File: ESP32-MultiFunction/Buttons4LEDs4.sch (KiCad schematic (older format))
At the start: 0 parts

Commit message: Working on ESP32-MultiFunction.
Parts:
- added C12: .1 uf, Capacitors_SMD:C_0603, symbol C
- added C13, C14, C15, C16: 10 nf, Capacitors_SMD:C_0603, symbol C_Small
- added R15, R17, R19, R21: R, Resistors_THT:R_Axial_DIN0207_L6.3mm_D2.5mm_P7.62mm_Horizontal, symbol R
- added R16, R18, R20, R22: 1.5K Ohms, Resistors_SMD:R_0603, symbol R
- added R23, R24, R25, R26: 10K Ohms, Resistors_SMD:R_0603, symbol R
- added Term6: +12 1 2 3 4 GND, Connectors_Terminal_Blocks:TerminalBlock_Pheonix_MPT-2.54mm_6pol, symbol Screw_Terminal_01x06
- added Term7: 1 2 3 4 GND, Connectors_Terminal_Blocks:TerminalBlock_Pheonix_MPT-2.54mm_5pol, symbol Screw_Terminal_01x05
- added U11, U12: TC4426, Housings_SOIC:SOIC-8_3.9x4.9mm_Pitch1.27mm, symbol TC4426
- added U13: 74HCT14, Housings_SOIC:SOIC-14_3.9x8.7mm_Pitch1.27mm, symbol 74HC14
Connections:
- new net: C13.1, R23.2, Term7.1 (Pin_1), U13.5
- new net: C14.1, R24.2, Term7.2 (Pin_2), U13.9
- new net: C16.1, R26.2, Term7.3 (Pin_3), U13.11
- new net: C15.1, R25.2, Term7.4 (Pin_4), U13.13
- new net: R15.2, R16.2, U11.7 (Out)
- new net: R17.2, R18.2, U11.5 (Out)
- new net: R19.2, R20.2, U12.7 (Out)
- new net: R21.2, R22.2, U12.5 (Out)
- new net: R15.1, R16.1, Term6.2 (Pin_2)
- new net: R17.1, R18.1, Term6.3 (Pin_3)
- new net: R19.1, R20.1, Term6.4 (Pin_4)
- new net: R21.1, R22.1, Term6.5 (Pin_5)
- new net +12V: Term6.1 (Pin_1), U11.6 (Vdd), U11.6 (Vdd), U12.6 (Vdd), U12.6 (Vdd)
- new net +3V3: R23.1, R24.1, R25.1, R26.1, U13.14 (VCC), U13.14 (VCC), U13.14 (VCC), U13.14 (VCC), U13.14 (VCC), U13.14 (VCC)
- new net Button1: U13.6
- new net Button2: U13.8
- new net Button3: U13.10
- new net Button4: U13.12
- new net GND: C12.2, C13.2, C14.2, C15.2, C16.2, Term6.6 (Pin_6), Term7.5 (Pin_5), U11.3 (GND), U11.3 (GND), U12.3 (GND), U12.3 (GND), U13.1, U13.3, U13.7 (GND), U13.7 (GND), U13.7 (GND), U13.7 (GND), U13.7 (GND), U13.7 (GND)
- new net LED1: U11.2 (IN)
- new net LED2: U11.4 (IN)
- new net LED3: U12.2 (IN)
- new net LED4: U12.4 (IN)
- no-connect marks 0 -> 2

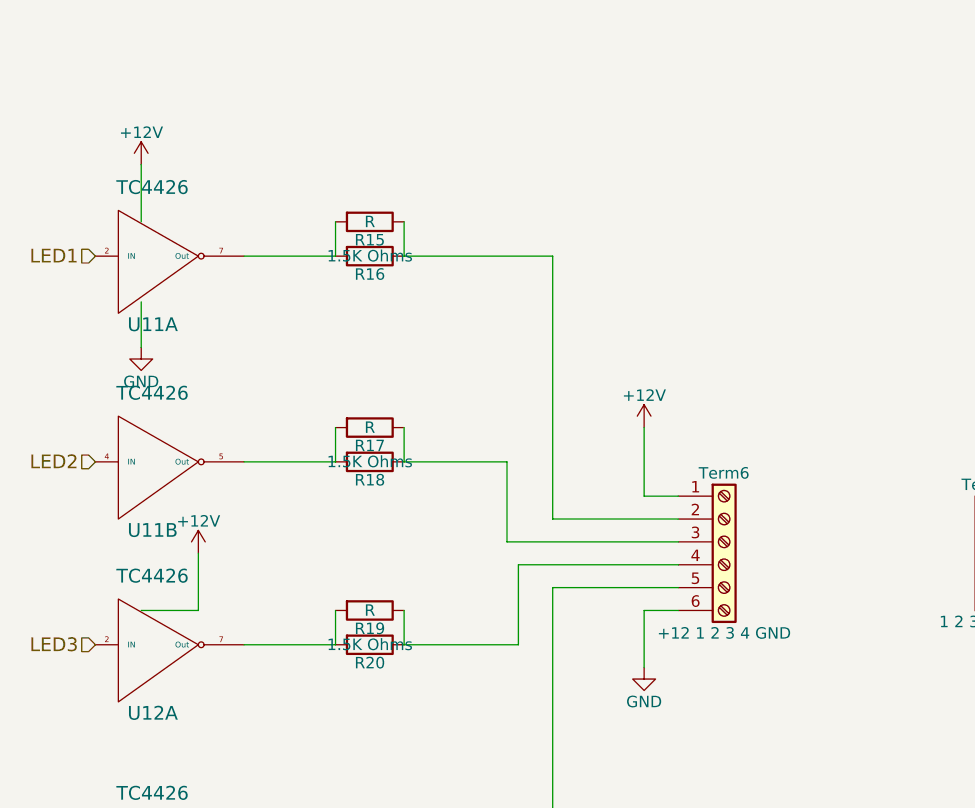
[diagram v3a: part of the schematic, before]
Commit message: Trying to isolate the 4 driver outputs.
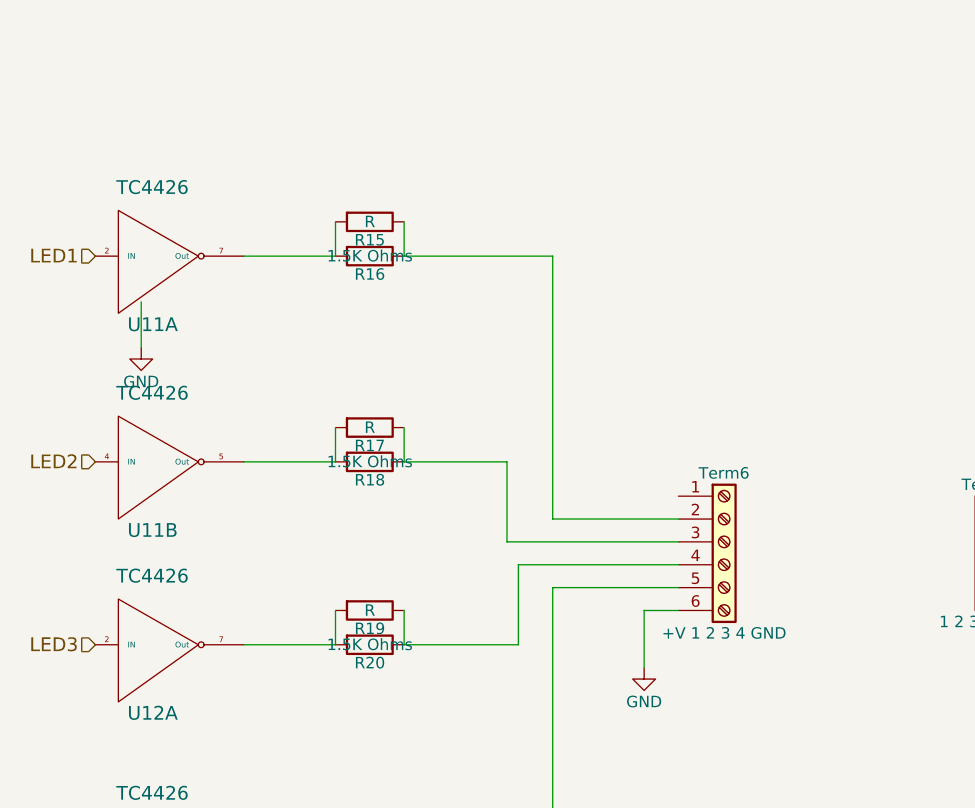
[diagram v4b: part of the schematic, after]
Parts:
- Term6: value +12 1 2 3 4 GND -> +V 1 2 3 4 GND
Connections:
- net labels removed: +12V
- wire segments 67 -> 62

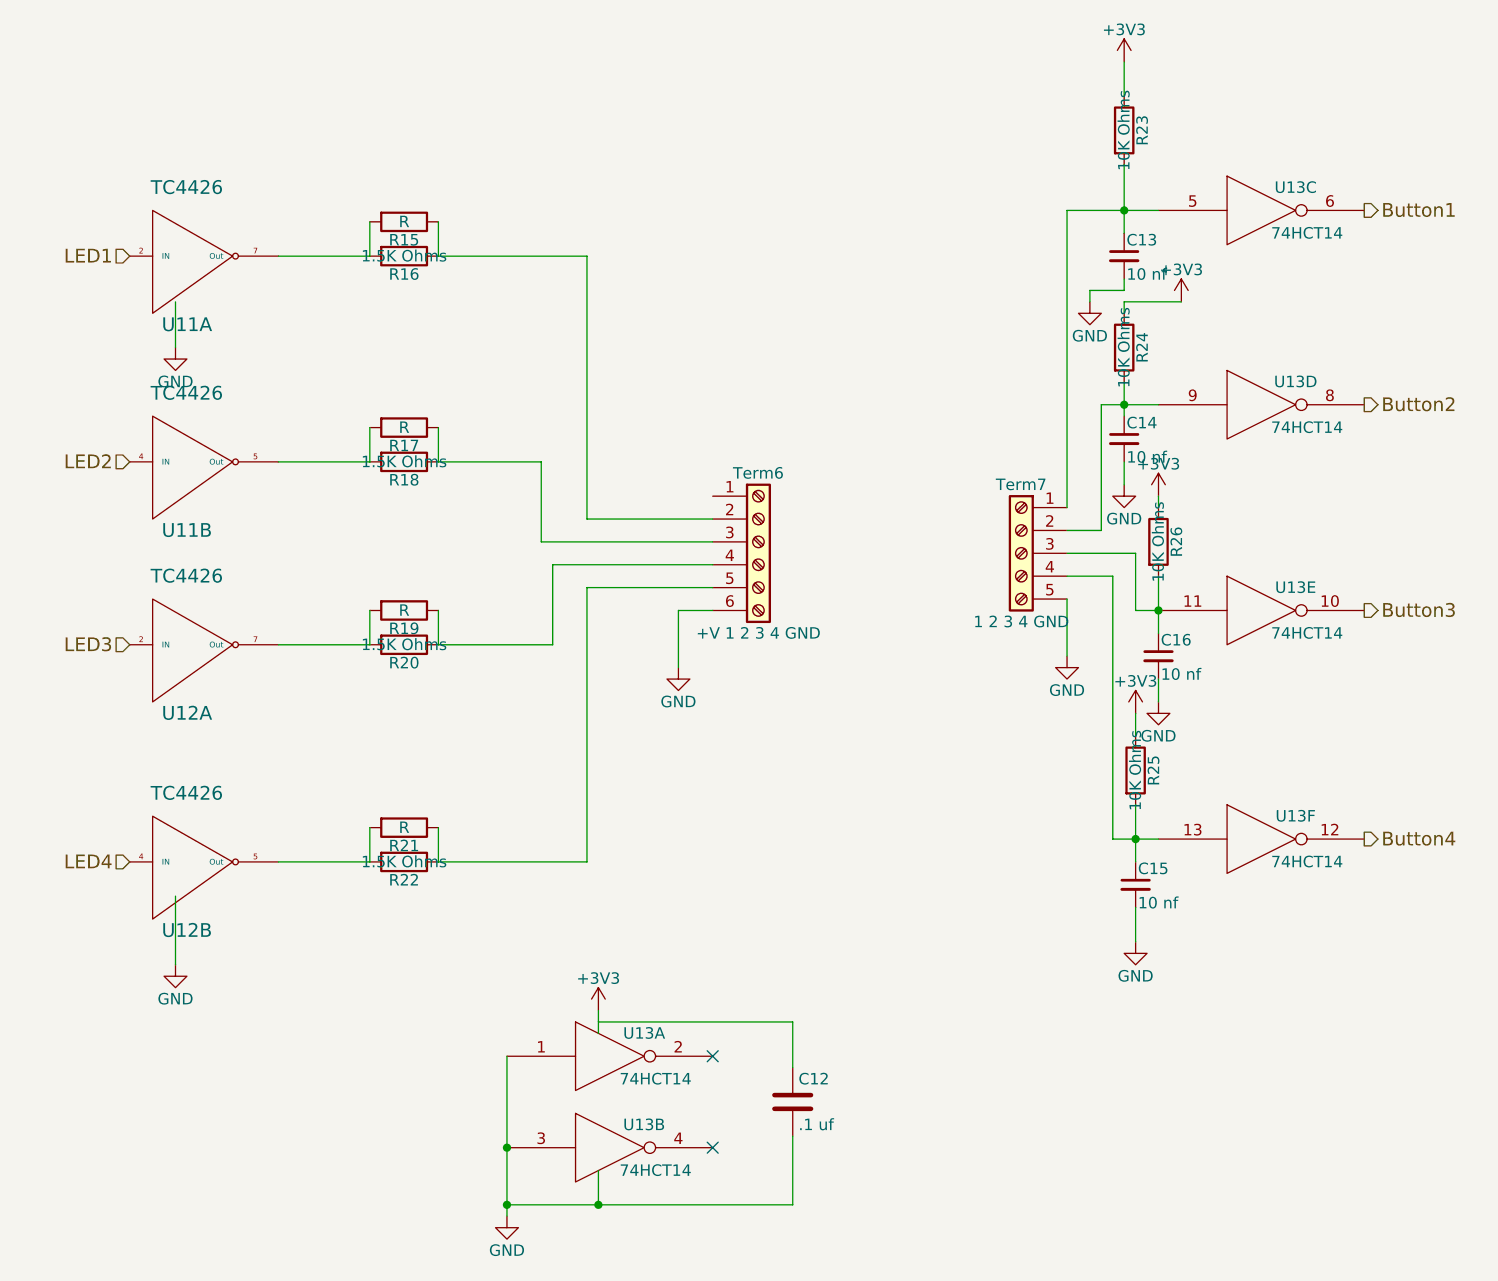
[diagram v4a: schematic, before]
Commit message: Isolate the AUX LED/device buffer power.
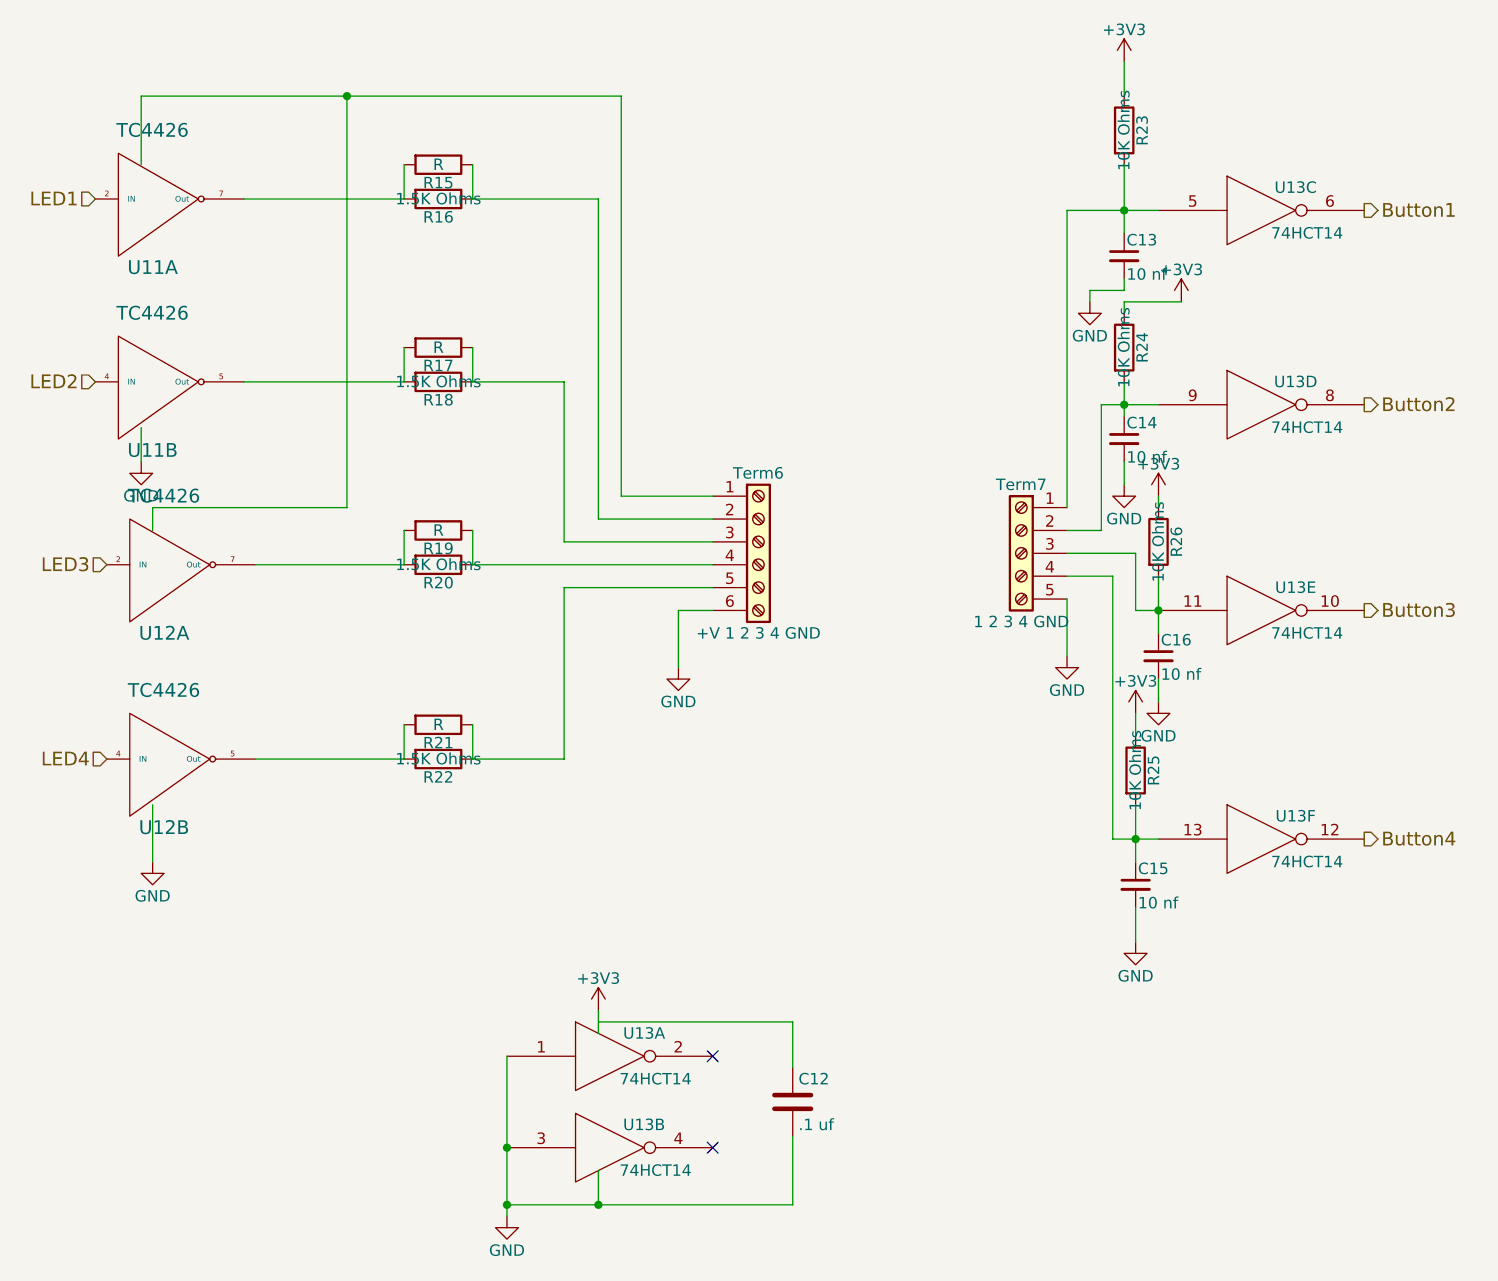
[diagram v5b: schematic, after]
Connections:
- wire segments 62 -> 67
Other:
- moved on the sheet: R15, R16, R17, R18, R19, R20, R21, R22, U11A, U11B, U12A, U12B

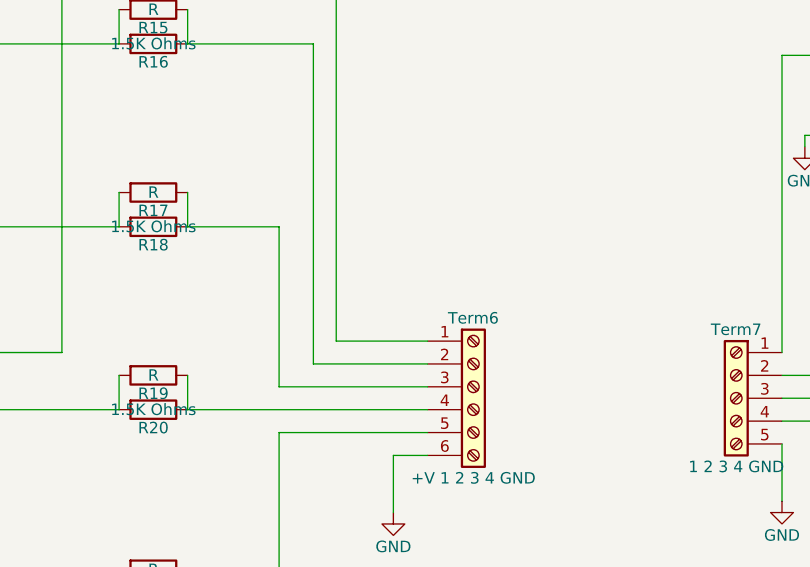
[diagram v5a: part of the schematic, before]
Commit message: Add I2C pullups to ESP32-MultiFunction.
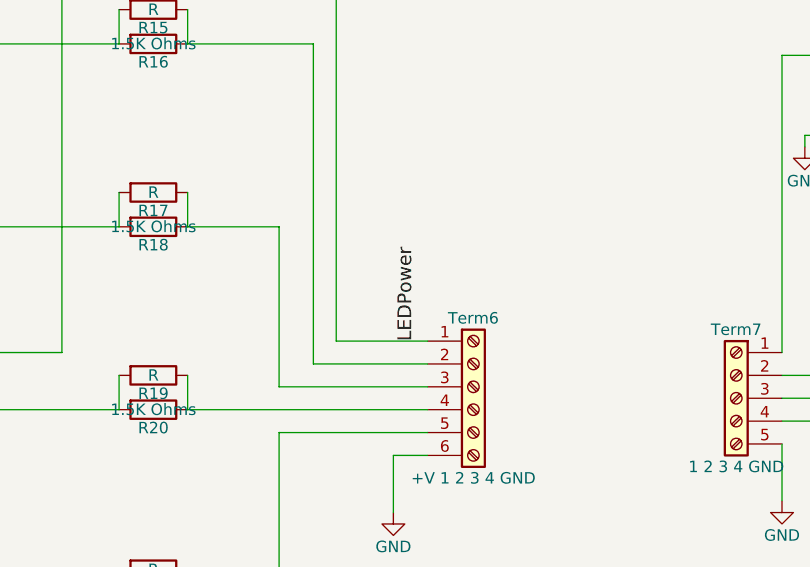
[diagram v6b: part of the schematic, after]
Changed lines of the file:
@@
 $EndComp
 $Comp
-L GND #PWR053
+L GND #PWR054
 U 1 1 60CEBBCA
 P 4750 3850
-F 0 "#PWR053" H 4750 3600 50  0001 C CNN
+F 0 "#PWR054" H 4750 3600 50  0001 C CNN
 F 1 "GND" H 4750 3700 50  0000 C CNN
 F 2 "" H 4750 3850 50  0001 C CNN
@@
 $EndComp
 $Comp
-L GND #PWR054
+L GND #PWR055
 U 1 1 60CEC8C9
 P 4000 6250
-F 0 "#PWR054" H 4000 6000 50  0001 C CNN
+F 0 "#PWR055" H 4000 6000 50  0001 C CNN
 F 1 "GND" H 4000 6100 50  0000 C CNN
 F 2 "" H 4000 6250 50  0001 C CNN
@@
 NoConn ~ 4900 5950
 $Comp
-L +3V3 #PWR055
+L +3V3 #PWR056
 U 1 1 60CECA8D
 P 4400 5350
-F 0 "#PWR055" H 4400 5200 50  0001 C CNN
+F 0 "#PWR056" H 4400 5200 50  0001 C CNN
 F 1 "+3V3" H 4400 5490 50  0000 C CNN
 F 2 "" H 4400 5350 50  0001 C CNN
@@
 $EndComp
 $Comp
-L GND #PWR056
+L GND #PWR057
 U 1 1 60CEE082
 P 6450 3800
-F 0 "#PWR056" H 6450 3550 50  0001 C CNN
+F 0 "#PWR057" H 6450 3550 50  0001 C CNN
 F 1 "GND" H 6450 3650 50  0000 C CNN
 F 2 "" H 6450 3800 50  0001 C CNN
@@
 $EndComp
 $Comp
-L +3V3 #PWR057
+L +3V3 #PWR058
 U 1 1 60CF063B
 P 6700 1200
-F 0 "#PWR057" H 6700 1050 50  0001 C CNN
+F 0 "#PWR058" H 6700 1050 50  0001 C CNN
 F 1 "+3V3" H 6700 1340 50  0000 C CNN
 F 2 "" H 6700 1200 50  0001 C CNN
@@
 $EndComp
 $Comp
-L +3V3 #PWR058
+L +3V3 #PWR059
 U 1 1 60CF0689
 P 6950 2250
-F 0 "#PWR058" H 6950 2100 50  0001 C CNN
+F 0 "#PWR059" H 6950 2100 50  0001 C CNN
 F 1 "+3V3" H 6950 2390 50  0000 C CNN
 F 2 "" H 6950 2250 50  0001 C CNN
@@
 $EndComp
 $Comp
-L +3V3 #PWR059
+L +3V3 #PWR060
 U 1 1 60CF0833
 P 6850 3100
-F 0 "#PWR059" H 6850 2950 50  0001 C CNN
+F 0 "#PWR060" H 6850 2950 50  0001 C CNN
 F 1 "+3V3" H 6850 3240 50  0000 C CNN
 F 2 "" H 6850 3100 50  0001 C CNN
@@
 $EndComp
 $Comp
-L +3V3 #PWR060
+L +3V3 #PWR061
 U 1 1 60CF0A78
 P 6750 4050
-F 0 "#PWR060" H 6750 3900 50  0001 C CNN
+F 0 "#PWR061" H 6750 3900 50  0001 C CNN
 F 1 "+3V3" H 6750 4190 50  0000 C CNN
 F 2 "" H 6750 4050 50  0001 C CNN
@@
 $EndComp
 $Comp
-L GND #PWR061
+L GND #PWR062
 U 1 1 60CF0DB8
 P 6550 2250
-F 0 "#PWR061" H 6550 2000 50  0001 C CNN
+F 0 "#PWR062" H 6550 2000 50  0001 C CNN
 F 1 "GND" H 6550 2100 50  0000 C CNN
 F 2 "" H 6550 2250 50  0001 C CNN
@@
 $EndComp
 $Comp
-L GND #PWR062
+L GND #PWR063
 U 1 1 60CF0EEE
 P 6700 3050
-F 0 "#PWR062" H 6700 2800 50  0001 C CNN
+F 0 "#PWR063" H 6700 2800 50  0001 C CNN
 F 1 "GND" H 6700 2900 50  0000 C CNN
 F 2 "" H 6700 3050 50  0001 C CNN
@@
 $EndComp
 $Comp
-L GND #PWR063
+L GND #PWR064
 U 1 1 60CF1041
 P 6850 4000
-F 0 "#PWR063" H 6850 3750 50  0001 C CNN
+F 0 "#PWR064" H 6850 3750 50  0001 C CNN
 F 1 "GND" H 6850 3850 50  0000 C CNN
 F 2 "" H 6850 4000 50  0001 C CNN
@@
 $EndComp
 $Comp
-L GND #PWR064
+L GND #PWR065
 U 1 1 60CF113D
 P 6750 5050
-F 0 "#PWR064" H 6750 4800 50  0001 C CNN
+F 0 "#PWR065" H 6750 4800 50  0001 C CNN
 F 1 "GND" H 6750 4900 50  0000 C CNN
 F 2 "" H 6750 5050 50  0001 C CNN
@@
 $EndComp
 $Comp
-L GND #PWR065
+L GND #PWR066
 U 1 1 6170C9FF
 P 2400 2950
-F 0 "#PWR065" H 2400 2700 50  0001 C CNN
+F 0 "#PWR066" H 2400 2700 50  0001 C CNN
 F 1 "GND" H 2400 2800 50  0000 C CNN
 F 2 "" H 2400 2950 50  0001 C CNN
@@
 $EndComp
 $Comp
-L GND #PWR066
+L GND #PWR067
 U 1 1 6170CA55
 P 2450 4700
-F 0 "#PWR066" H 2450 4450 50  0001 C CNN
+F 0 "#PWR067" H 2450 4450 50  0001 C CNN
 F 1 "GND" H 2450 4550 50  0000 C CNN
 F 2 "" H 2450 4700 50  0001 C CNN
@@
 Wire Wire Line
 	2450 4700 2450 4450
+Text Label 4850 3100 1    60   ~ 0
+LEDPower
 $EndSCHEMATC
